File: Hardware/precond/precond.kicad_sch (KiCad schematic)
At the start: 29 parts, among them J1 Conn_Coaxial, J2 Conn_Coaxial, J3 Buck_logic_in, J4 3.3V_header, Q1 PMOS, U1 OPA2340, U2 OPA2340

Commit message: stuff 2
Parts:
- added R5: 1k, symbol Device:R
- renumbered Rs to Rs2
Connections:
- net +5V: now also R5.1
- net at Q1.2 (G): now also R5.2; no longer J3.1 (Pin_1)
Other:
- moved on the sheet: J3

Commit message: for adam
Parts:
- removed D2, D4, D6, D7: D_Schottky, symbol Device:D_Schottky
- removed Q1: PMOS, symbol Simulation_SPICE:PMOS
- added C5: 220uF, Capacitor_SMD:C_0805_2012Metric, symbol Device:C_Polarized
- added D10, D11, D8, D9: 1N5819, Diode_THT:D_DO-41_SOD81_P10.16mm_Horizontal, symbol Diode:1N5819
- added Q2: AO3401A, Package_TO_SOT_SMD:SOT-23, symbol Transistor_FET:AO3401A
- added Q3: FQP27P06, Package_TO_SOT_THT:TO-220-3_Vertical, symbol Transistor_FET:FQP27P06
- added R6, R8: 1k, Resistor_SMD:R_0805_2012Metric, symbol Device:R
- added R7: 22, Resistor_SMD:R_0805_2012Metric, symbol Device:R
- C1: footprint (none) -> Capacitor_SMD:C_0805_2012Metric
- C2: value 220uF -> 1n; footprint (none) -> Capacitor_SMD:C_0805_2012Metric
- C3, C4: footprint (none) -> Capacitor_THT:CP_Radial_D8.0mm_P3.80mm
- D1, D5: footprint (none) -> Diode_THT:D_DO-15_P10.16mm_Horizontal
- J1: footprint (none) -> onnector_Coaxial:SMA_Amphenol_132134-11_Vertical
- J2: footprint (none) -> Connector_Coaxial:SMA_Amphenol_132134-11_Vertical
- J3, J4: footprint (none) -> Connector_PinHeader_1.00mm:PinHeader_1x02_P1.00mm_Vertical
- L1: value 33uH -> 470uH; footprint (none) -> Inductor_THT:L_Radial_D10.0mm_P5.00mm_Fastron_07M
- R1, R2, R3, R4, Rf1, Rg1, Rs2: footprint (none) -> R_Axial_DIN0207_L6.3mm_D2.5mm_P7.62mm_Horizontal
- R5: footprint (none) -> Resistor_SMD:R_0805_2012Metric
- Rf2, Rg2, Rs1: footprint (none) -> Resistor_THT:R_Axial_DIN0207_L6.3mm_D2.5mm_P7.62mm_Horizontal
- U1, U2: footprint (none) -> Package_DIP:DIP-8_W7.62mm
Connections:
- net +3.3V: now also C5.1, R8.1; no longer C2.1
- net +5V: now also Q3.3 (S)
- net GND: now also C5.2, D10.1 (K), D11.1 (K), D8.1 (K), D9.1 (K), R8.2
- net at Rf2.1, Rg2.2, U2.2 (-): now also D10.2 (A), D11.2 (A)
- net at D3.1 (K), L1.1: now also Q3.2 (D), R7.1
- net at R5.2: now also Q2.3 (D)
- net at Rf1.1, Rg1.2, U1.2 (-): now also D8.2 (A), D9.2 (A)
- net at J3.1 (Pin_1): now also R6.2
- new net: Q2.1 (G), R6.1
- new net: Q2.2 (S), Q3.1 (G)
- new net: C2.1, R7.2
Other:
- moved on the sheet: C1, C2, D3, J3, J4, L1, R5

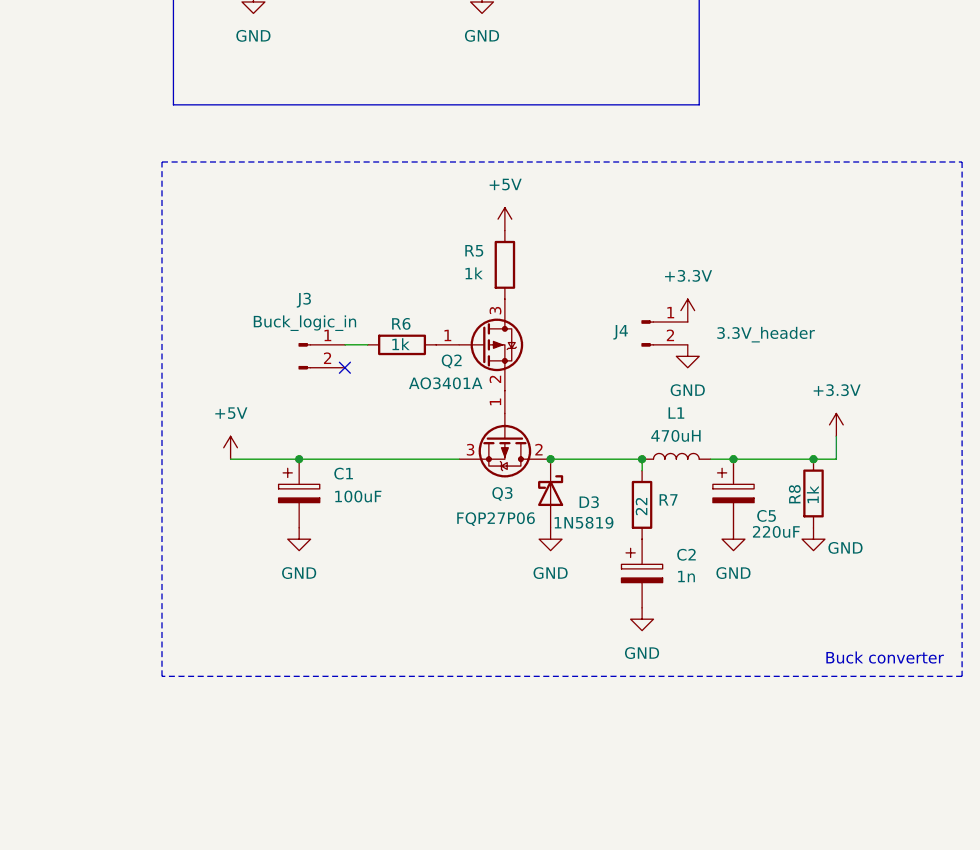
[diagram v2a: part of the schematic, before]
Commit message: update schematic with new transistors
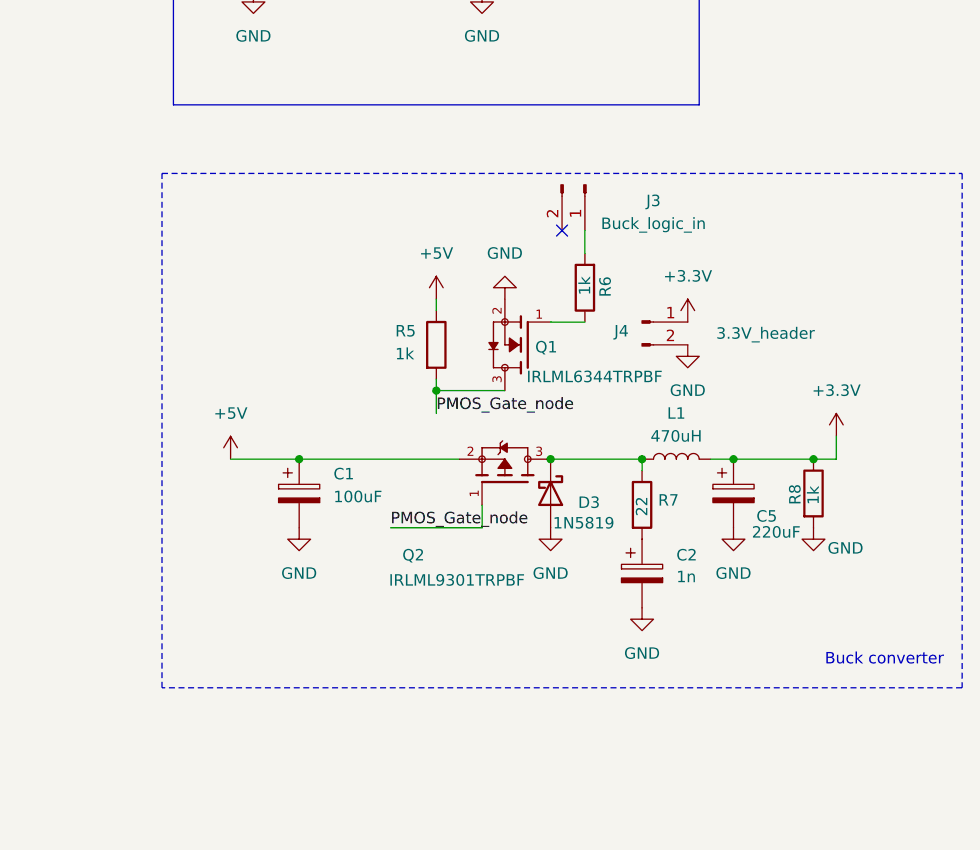
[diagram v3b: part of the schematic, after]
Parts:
- removed Q2: AO3401A, Package_TO_SOT_SMD:SOT-23, symbol Transistor_FET:AO3401A
- removed Q3: FQP27P06, Package_TO_SOT_THT:TO-220-3_Vertical, symbol Transistor_FET:FQP27P06
- added Q1: IRLML6344TRPBF, IRLML6344TRPBF:TRANS_IRLML6344TRPBF, symbol precond_lib:IRLML6344TRPBF
- added Q2: IRLML9301TRPBF, IRLML9301TRPBF:SOT95P237X112-3N, symbol precond_lib:IRLML9301TRPBF
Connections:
- net +5V: now also Q2.2
- net GND: now also Q1.2
- net at R6.1: now also Q1.1
- net at D3.1 (K), L1.1, R7.1: now also Q2.3
- net PMOS_Gate_node: now reaches R5.2
- net PMOS_Gate_node: now also Q1.3, Q2.1
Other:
- moved on the sheet: J3, R5, R6

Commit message: wip
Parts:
- added A1: RaspberryPi_Pico, Module:RaspberryPi_Pico_Common_Unspecified, symbol MCU_Module:RaspberryPi_Pico
- added J5: AMS_Conn, symbol Connector_Generic:Conn_02x10_Odd_Even
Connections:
- net +5V: now also A1.40 (VBUS), J5.13 (Pin_13)
- net GND: now also A1.13 (GND), A1.18 (GND), A1.23 (GND), A1.28 (GND), A1.3 (GND), A1.33 (AGND), A1.38 (GND), A1.8 (GND), J5.3 (Pin_3), J5.4 (Pin_4), J5.5 (Pin_5), J5.8 (Pin_8)
- net Op0.5V_1: no longer U2.3 (+), U2.6 (-), U2.7
- net Op2_out: now reaches Rf2.2, U2.1
- net Op2_out: now also J5.7 (Pin_7)
- net Op1_out: now reaches Rf1.2, U1.1
- net Op1_out: now also J5.6 (Pin_6)
- new net Op0.5_2: U2.3 (+), U2.6 (-), U2.7

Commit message: footprints and stuff
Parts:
- removed A1: RaspberryPi_Pico, Module:RaspberryPi_Pico_Common_Unspecified, symbol MCU_Module:RaspberryPi_Pico
- added C6: 47uF, Capacitor_THT:CP_Radial_D8.0mm_P3.50mm, symbol Device:C_Polarized
- C1, C5: footprint Capacitor_SMD:C_0805_2012Metric -> Capacitor_THT:CP_Radial_D8.0mm_P3.80mm
- C3, C4: footprint Capacitor_THT:CP_Radial_D8.0mm_P3.80mm -> Capacitor_THT:C_Rect_L7.2mm_W2.5mm_P5.00mm_FKS2_FKP2_MKS2_MKP2
- J1: footprint onnector_Coaxial:SMA_Amphenol_132134-11_Vertical -> Connector_Coaxial:BNC_Amphenol_B6252HB-NPP3G-50_Horizontal
- J2: footprint Connector_Coaxial:SMA_Amphenol_132134-11_Vertical -> Connector_Coaxial:BNC_Amphenol_B6252HB-NPP3G-50_Horizontal
- J3, J4: footprint Connector_PinHeader_1.00mm:PinHeader_1x02_P1.00mm_Vertical -> Connector_JST:JST_PH_B2B-PH-K_1x02_P2.00mm_Vertical
- J5: footprint (none) -> Connector_PinHeader_2.54mm:PinHeader_2x10_P2.54mm_Horizontal
- Q1: footprint IRLML6344TRPBF:TRANS_IRLML6344TRPBF -> Package_TO_SOT_SMD:SOT-23-3
- Q2: footprint IRLML9301TRPBF:SOT95P237X112-3N -> Package_TO_SOT_SMD:SOT-23-3
- R1, R2, R3, R4, Rf1, Rg1, Rs2: footprint R_Axial_DIN0207_L6.3mm_D2.5mm_P7.62mm_Horizontal -> Resistor_THT:R_Axial_DIN0207_L6.3mm_D2.5mm_P7.62mm_Horizontal
- U1, U2: footprint Package_DIP:DIP-8_W7.62mm -> Package_SO:SOIC-8-1EP_3.9x4.9mm_P1.27mm_EP2.29x3mm
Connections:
- net +5V: now also C6.1
- net GND: now also C6.2
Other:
- added sheet Raspberry Pi Pico UART module (uart.kicad_sch)
- moved on the sheet: C1, C2, C5, D3, J3, J4, J5, L1, Q1, Q2, R5, R6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

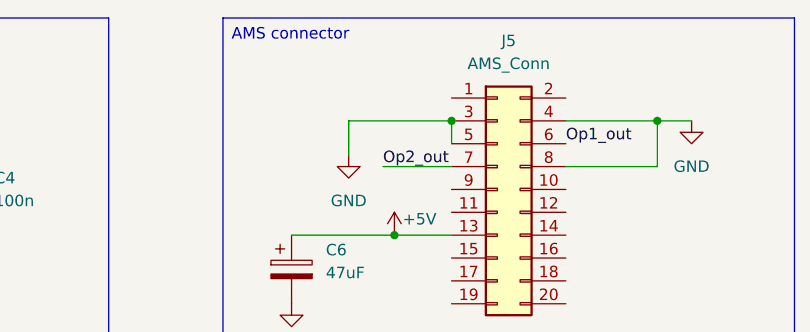
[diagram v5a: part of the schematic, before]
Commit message: fixed ams conn trust
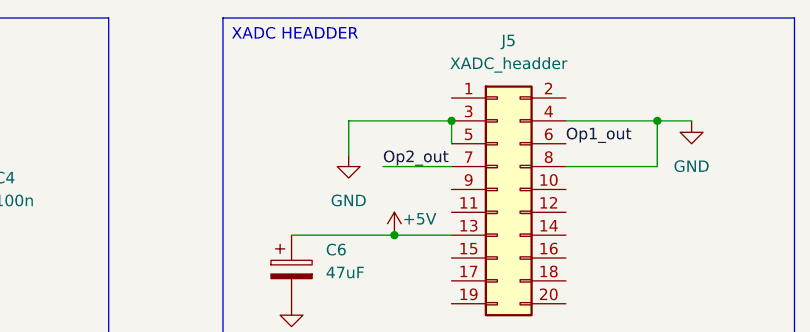
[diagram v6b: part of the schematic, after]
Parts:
- J5: value AMS_Conn -> XADC_headder; footprint Connector_PinHeader_2.54mm:PinHeader_2x10_P2.54mm_Horizontal -> Connector_PinSocket_2.00mm:PinSocket_2x10_P2.00mm_Vertical
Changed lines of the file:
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@@
 		)
 	)
-	(text_box "AMS connector\n"
+	(text_box "XADC HEADDER\n"
 		(exclude_from_sim no)
 		(at 203.2 25.4 0)
@@
 			)
 		)
-		(property "Value" "AMS_Conn"
+		(property "Value" "XADC_headder"
 			(at 234.95 30.48 0)
 			(effects
@@
 			)
 		)
-		(property "Footprint" "Connector_PinHeader_2.54mm:PinHeader_2x10_P2.54mm_Horizontal"
+		(property "Footprint" "Connector_PinSocket_2.00mm:PinSocket_2x10_P2.00mm_Vertical"
 			(at 233.68 44.45 0)
 			(effects
